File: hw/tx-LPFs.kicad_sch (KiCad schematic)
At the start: 74 parts, among them K1606 G5Q-14-05, K7701 G5Q-14-05, K7702 G5Q-14-05, K7703 G5Q-14-05, K7704 G5Q-14-05, K7705 G5Q-14-05, K7706 G5Q-14-05, K7707 G5Q-14-05, K7708 G5Q-14-05, K7709 G5Q-14-05, U1601 TPIC6C595PWR, U7701 TPIC6C595PWR

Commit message: I think I have finished the relay conversion and 5V SPI I/O expander crap
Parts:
- renumbered C7707 to C7848, C7703 to C7849, C7704 to C7850, C7705 to C7851, C7706 to C7852, C1605 to C7853, C1606 to C7854, C1607 to C7855, C1609 to C7856, C1608 to C7857, C1610 to C7858, C1611 to C7859, C1612 to C7860, C1613 to C7861, C1614 to C7862, C1615 to C7863, C1616 to C7864, C1617 to C7865, C1618 to C7866, C1619 to C7867, C1620 to C7868, C1621 to C7869, C1622 to C7870, C1623 to C7871, C1624 to C7872, C1627 to C7873, C1625 to C7874, C1626 to C7875, C1629 to C7876, C1628 to C7877, C1630 to C7878, C1631 to C7879, C1632 to C7880, C1634 to C7881, C1633 to C7882, C7708 to C7883, C7709 to C7884, C7710 to C7885, C7711 to C7886, C7712 to C7887, C1604 to C7888, C7702 to C7889, K7703 to K7708, K1606 to K7709, K7701 to K7710, K7702 to K7711, K7704 to K7712, K7705 to K7713, K7706 to K7714, K7707 to K7715, K7708 to K7716, K7709 to K7717, L1602 to L7705, L1601 to L7706, L1603 to L7707, L1605 to L7708, L1604 to L7709, L1607 to L7710, L1606 to L7711, L1609 to L7712, L1608 to L7713, L1611 to L7714, L1610 to L7715, L1612 to L7716, L1613 to L7717, L1614 to L7718, L1615 to L7719, L1617 to L7720, L1616 to L7721, L1618 to L7722, L1619 to L7723, L1620 to L7724, U1601 to U7739, U7701 to U7740

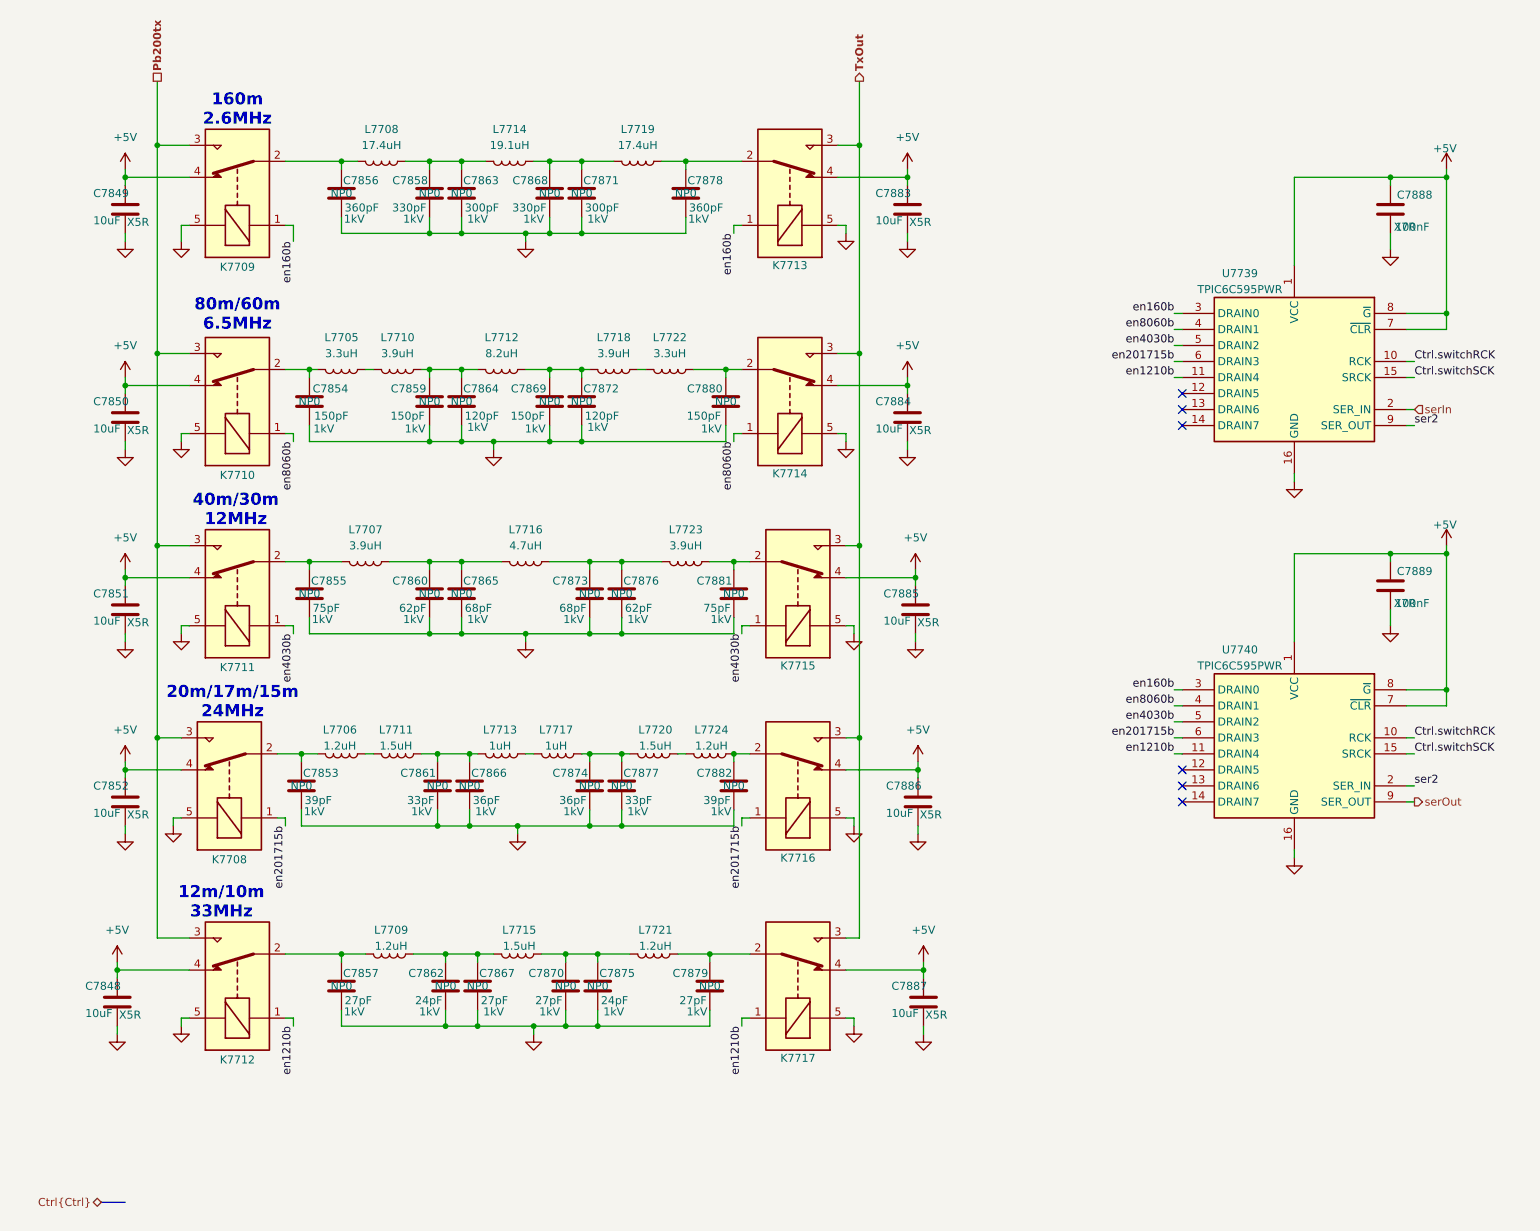
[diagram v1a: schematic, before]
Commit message: Starting to build guanella transformers. Mostly converted to 1-2-1 tx, but FPGA still to do.
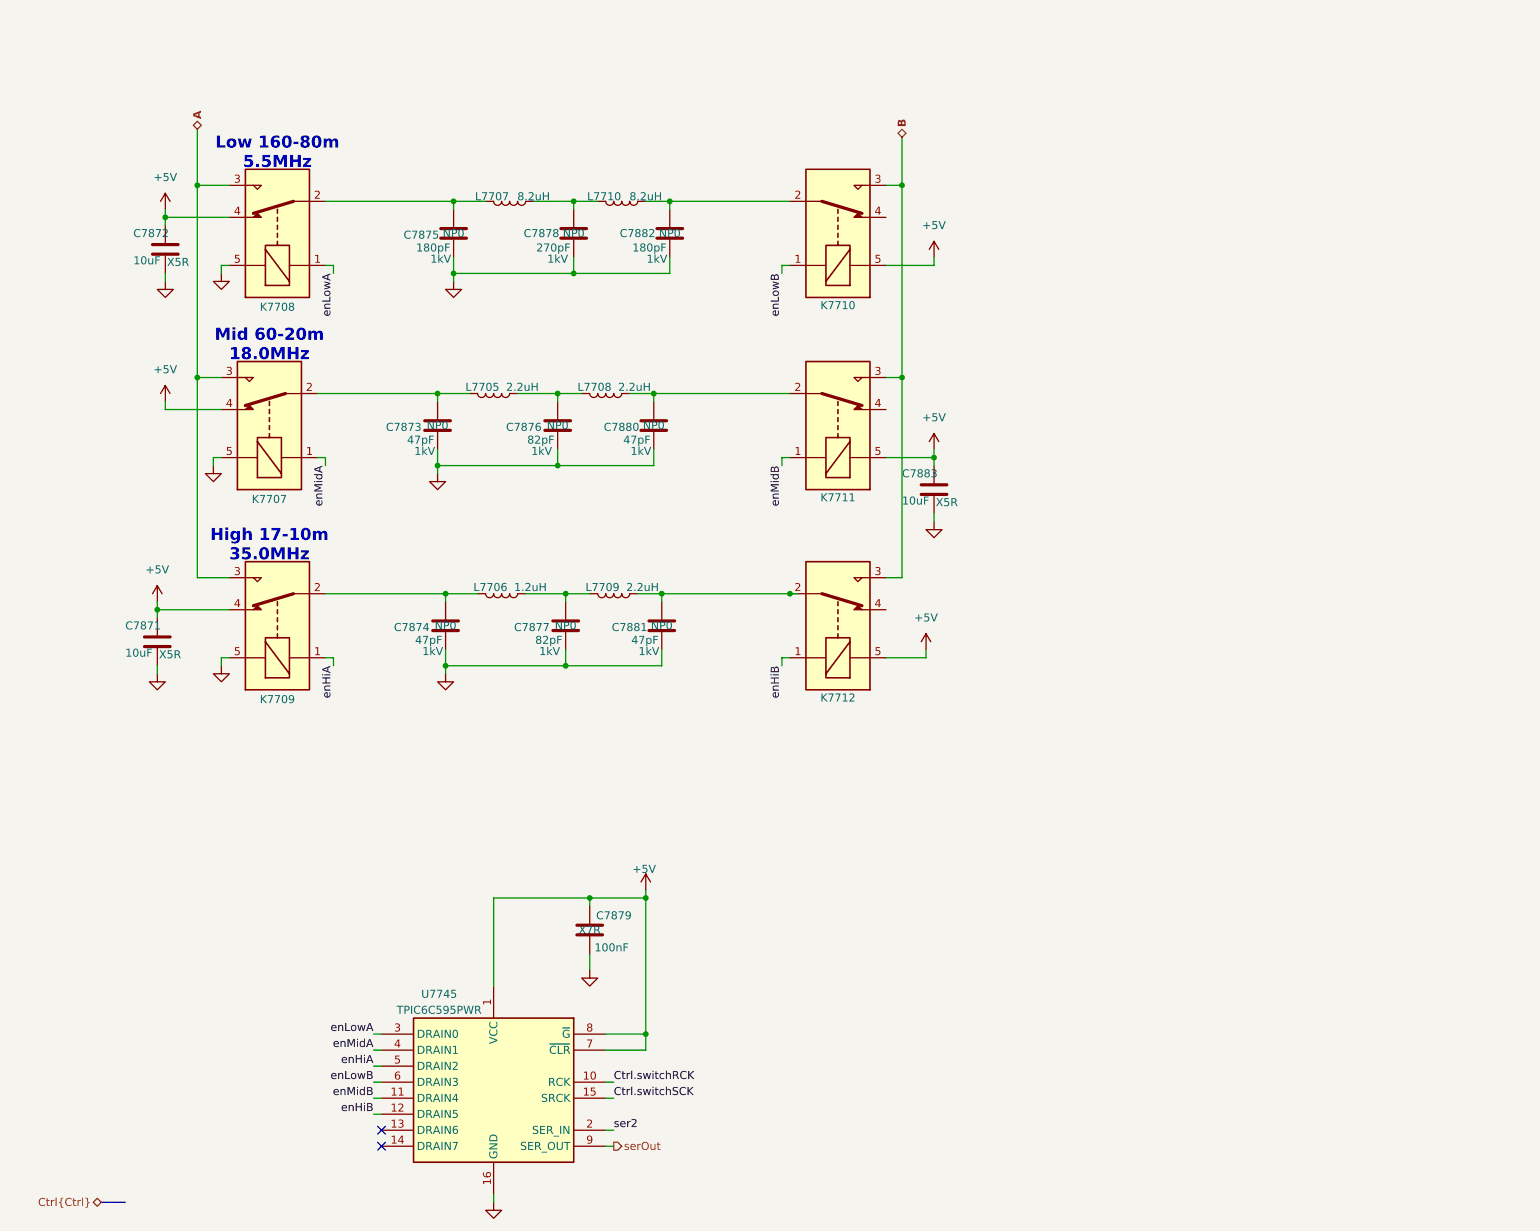
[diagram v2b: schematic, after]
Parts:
- removed C7849, C7850, C7852, C7883, C7884, C7885, C7887: 10uF, Capacitor_SMD:C_0805_2012Metric, symbol Device:C
- removed C7853, C7882: 39pF, Capacitor_SMD:C_0201_0603Metric, symbol Device:C
- removed C7854, C7859, C7869: 150pF, Capacitor_SMD:C_0201_0603Metric, symbol Device:C
- removed C7856, C7878: 360pF, Capacitor_SMD:C_0201_0603Metric, symbol Device:C
- removed C7857, C7867, C7870, C7879: 27pF, Capacitor_SMD:C_0201_0603Metric, symbol Device:C
- removed C7858, C7868: 330pF, Capacitor_SMD:C_0201_0603Metric, symbol Device:C
- removed C7861: 33pF, Capacitor_SMD:C_0201_0603Metric, symbol Device:C
- removed C7862, C7875: 24pF, Capacitor_SMD:C_0201_0603Metric, symbol Device:C
- removed C7863, C7871: 300pF, Capacitor_SMD:C_0201_0603Metric, symbol Device:C
- removed C7864, C7872: 120pF, Capacitor_SMD:C_0201_0603Metric, symbol Device:C
- removed C7865: 68pF, Capacitor_SMD:C_0201_0603Metric, symbol Device:C
- removed C7866: 36pF, Capacitor_SMD:C_0201_0603Metric, symbol Device:C
- removed C7888: 100nF, Capacitor_SMD:C_0805_2012Metric, symbol Device:C
- removed K7709, K7710, K7713, K7714: G5Q-14-05, Relay_THT:Relay_SPDT_Omron-G5Q-1, symbol Relay:G5Q-1
- removed L7710, L7718: 3.9uH, Library:L_Wurth_12.1mm_sq_SMT, symbol Device:L
- removed L7711, L7715, L7720: 1.5uH, Inductor_SMD:L_1812_4532Metric, symbol Device:L
- removed L7712: 8.2uH, Library:L_Wurth_10.9mm_sq_SMT, symbol Device:L
- removed L7713, L7717: 1uH, Inductor_SMD:L_1812_4532Metric, symbol Device:L
- removed L7714: 19.1uH, Library:toroid-inductor-t80-2, symbol Device:L
- removed L7716: 4.7uH, Library:L_Wurth_8.4mm_sq_SMT, symbol Device:L
- removed L7719: 17.4uH, Library:toroid-inductor-t80-2, symbol Device:L
- removed L7721, L7724: 1.2uH, Inductor_SMD:L_1812_4532Metric, symbol Device:L
- removed L7722: 3.3uH, Library:L_Wurth_8.4mm_sq_SMT, symbol Device:L
- removed U7739: TPIC6C595PWR, SOP65P640X120-16N, symbol Library:TPIC6C595PWR
- added C7881: 47pF, Capacitor_SMD:C_0201_0603Metric, symbol Device:C
- C7873: value 68pF -> 47pF
- C7874: value 36pF -> 47pF
- C7875: renamed from C7855; value 75pF -> 180pF
- C7876: value 62pF -> 82pF
- C7877: value 33pF -> 82pF
- C7878: renamed from C7860; value 62pF -> 270pF
- C7880: value 150pF -> 47pF
- C7882: renamed from C7881; value 75pF -> 180pF
- L7705: value 3.3uH -> 2.2uH; footprint Library:L_Wurth_8.4mm_sq_SMT -> Library:L_Wurth_12.1mm_sq_SMT; MP 7443340330 -> 7443310390
- L7706: footprint Inductor_SMD:L_1812_4532Metric -> Library:L_Wurth_12.1mm_sq_SMT; MF Coilcraft -> Wurth; MP 1812FS-122JR_ -> 7443310390
- L7707: value 3.9uH -> 8.2uH
- L7708: value 17.4uH -> 2.2uH; footprint Library:toroid-inductor-t80-2 -> Library:L_Wurth_12.1mm_sq_SMT; MF (none) -> Wurth; MP (none) -> 7443310390
- L7709: value 1.2uH -> 2.2uH; footprint Inductor_SMD:L_1812_4532Metric -> Library:L_Wurth_12.1mm_sq_SMT; MF Coilcraft -> Wurth; MP 1812FS-122JR -> 7443310390; Mfg Wurth -> (none); MfgPart 74433300180 -> (none)
- L7710: renamed from L7723; value 3.9uH -> 8.2uH
- renumbered C7848 to C7871, C7851 to C7872, C7889 to C7879, C7886 to C7883, K7708 to K7707, K7711 to K7708, K7712 to K7709, K7715 to K7710, K7716 to K7711, K7717 to K7712, U7740 to U7745
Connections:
- net +5V: now also K7710.5, K7711.5, K7712.5; no longer K7710.4, K7711.4, K7712.4
- net GND: now also C7881.2; no longer K7710.5, K7711.5, K7712.5
- net at K7712.2: now also L7709.2, C7881.1
- net at C7878.1, L7707.2: now also L7710.1
- net at C7877.1: now also L7706.2, L7709.1; no longer C7874.1
- net enHiB: now reaches U7745.12 (DRAIN5)
- net enHiB: now also K7712.1
- net at K7709.2: now also C7874.1, L7706.1; no longer L7709.1
- net at K7711.2: now also C7880.1, L7708.2
- net at L7708.1: now also C7876.1, L7705.2
- net at L7705.1: now also C7873.1, K7707.2
- net Pb200tx renamed A
- net TxOut renamed B
- removed net en1210b: K7709.1, K7712.1, U7745.11 (DRAIN4)
- net en160b renamed enLowA
- net enLowA: now also K7708.1
- removed net en201715b: K7707.1, K7711.1, U7745.6 (DRAIN3)
- removed net en4030b: K7708.1, K7710.1, U7745.5 (DRAIN2)
- net en8060b renamed enMidA
- net enMidA: now also K7707.1
- new net enHiA: K7709.1, U7745.5 (DRAIN2)
- new net enLowB: K7710.1, U7745.6 (DRAIN3)
- new net enMidB: K7711.1, U7745.11 (DRAIN4)
- no-connect marks 6 -> 2
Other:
- note added: "High 17-10m 35.0MHz"
- note added: "Low 160-80m 5.5MHz"
- note added: "Mid 60-20m 18.0MHz"
- note removed: "12m/10m 33MHz"
- note removed: "160m 2.6MHz"
- note removed: "20m/17m/15m 24MHz"
- note removed: "40m/30m 12MHz"
- note removed: "80m/60m 6.5MHz"
- moved on the sheet: C7871, C7872, C7875, C7878, C7879, C7882, C7883, K7707, K7708, K7709, K7710, K7711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

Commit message: Checkpoint. FPGA is mostly done (need a check!). Working on new LPFs. Need inductor footprints and to fix a bunch of broken/missing footprints.
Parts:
- C7873, C7875, C7876, C7878, C7880, C7882: footprint Capacitor_SMD:C_0201_0603Metric -> Capacitor_SMD:C_0603_1608Metric
- C7874, C7881: value 47pF -> 27pF; footprint Capacitor_SMD:C_0201_0603Metric -> Capacitor_SMD:C_0603_1608Metric
- C7877: value 82pF -> 47pF; footprint Capacitor_SMD:C_0201_0603Metric -> Capacitor_SMD:C_0603_1608Metric
- C7879: footprint Capacitor_SMD:C_0805_2012Metric -> Capacitor_SMD:C_0603_1608Metric
- L7705, L7706, L7708: footprint Library:L_Wurth_12.1mm_sq_SMT -> (none)
- L7707, L7710: footprint Library:L_Wurth_12.1mm_sq_SMT -> (none); MF Wurth -> (none); MP 7443310390 -> (none)
- L7709: value 2.2uH -> 1.2uH; footprint Library:L_Wurth_12.1mm_sq_SMT -> (none)

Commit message: OK I have part numbers for consolidated caps, resistors, inductors and all ICs are now Uxxx refdes.
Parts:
- C7882: renamed from C7871; footprint Capacitor_SMD:C_0805_2012Metric -> Capacitor_SMD:C_0603_1608Metric; Manufacturer_Name (none) -> Taoup Uidem; Manufacturer_Part_Number (none) -> 81-GXT155R71E223KE1D; Mouser Part Number (none) -> 963-MLAST168BB5106MT; working-voltage 10V -> 25V
- C7883: renamed from C7872; footprint Capacitor_SMD:C_0805_2012Metric -> Capacitor_SMD:C_0603_1608Metric; Manufacturer_Name (none) -> Taoup Uidem; Manufacturer_Part_Number (none) -> 81-GXT155R71E223KE1D; Mouser Part Number (none) -> 963-MLAST168BB5106MT; working-voltage 10V -> 25V
- C7884: renamed from C7873; footprint Capacitor_SMD:C_0603_1608Metric -> Capacitor_SMD:C_0805_2012Metric; Manufacturer_Name (none) -> YAGEO; Manufacturer_Part_Number (none) -> CC0805JRNPOCBN470; Mouser Part Number (none) -> 603-CC0805JRCBN470
- C7885: renamed from C7874; footprint Capacitor_SMD:C_0603_1608Metric -> Capacitor_SMD:C_0805_2012Metric; Manufacturer_Name (none) -> Kyocera AVX; Manufacturer_Part_Number (none) -> KGM21ECG3A270JU; Mouser Part Number (none) -> 581-KGM21ECG3A270JU
- C7886: renamed from C7875; footprint Capacitor_SMD:C_0603_1608Metric -> Capacitor_SMD:C_0805_2012Metric; Manufacturer_Name (none) -> KEMET; Manufacturer_Part_Number (none) -> C0805C181JDGACAUTO; Mouser Part Number (none) -> 80-C0805C181JDGACATO
- C7887: renamed from C7876; footprint Capacitor_SMD:C_0603_1608Metric -> Capacitor_SMD:C_0805_2012Metric; Manufacturer_Name (none) -> KEMET; Manufacturer_Part_Number (none) -> C0805C820JDGACTU; Mouser Part Number (none) -> 80-C0805C820JDG
- C7888: renamed from C7877; footprint Capacitor_SMD:C_0603_1608Metric -> Capacitor_SMD:C_0805_2012Metric; Manufacturer_Name (none) -> YAGEO; Manufacturer_Part_Number (none) -> CC0805JRNPOCBN470; Mouser Part Number (none) -> 603-CC0805JRCBN470
- C7889: renamed from C7878; Manufacturer_Name (none) -> TDK; Manufacturer_Part_Number (none) -> CGA3E2C0G1H271J080AA; Mouser Part Number (none) -> 810-CGA3E2C0G1H271J
- C7890: renamed from C7879; Manufacturer_Name (none) -> Kemet; Manufacturer_Part_Number (none) -> C0805F104K1RACAUTO; Mouser Part Number (none) -> 80-C0805F104K1RAUTO
- C7891: renamed from C7880; footprint Capacitor_SMD:C_0603_1608Metric -> Capacitor_SMD:C_0805_2012Metric; Manufacturer_Name (none) -> YAGEO; Manufacturer_Part_Number (none) -> CC0805JRNPOCBN470; Mouser Part Number (none) -> 603-CC0805JRCBN470
- C7892: renamed from C7881; footprint Capacitor_SMD:C_0603_1608Metric -> Capacitor_SMD:C_0805_2012Metric; Manufacturer_Name (none) -> Kyocera AVX; Manufacturer_Part_Number (none) -> KGM21ECG3A270JU; Mouser Part Number (none) -> 581-KGM21ECG3A270JU
- C7893: renamed from C7882; footprint Capacitor_SMD:C_0603_1608Metric -> Capacitor_SMD:C_0805_2012Metric; Manufacturer_Name (none) -> KEMET; Manufacturer_Part_Number (none) -> C0805C181JDGACAUTO; Mouser Part Number (none) -> 80-C0805C181JDGACATO
- C7894: renamed from C7883; footprint Capacitor_SMD:C_0805_2012Metric -> Capacitor_SMD:C_0603_1608Metric; Manufacturer_Name (none) -> Taoup Uidem; Manufacturer_Part_Number (none) -> 81-GXT155R71E223KE1D; Mouser Part Number (none) -> 963-MLAST168BB5106MT; working-voltage 10V -> 25V
- renumbered U7745 to U7744

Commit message: checkpoint to merge
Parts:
- L7705, L7707, L7708, L7710: footprint (none) -> Library:T68-toroid-1
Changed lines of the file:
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@@
 			)
 		)
-		(property "Footprint" ""
+		(property "Footprint" "Library:T68-toroid-1"
 			(at 86.36 71.12 0)
 			(effects
@@
 			)
 		)
-		(property "Description" "2.2uH T68-6 22t #18AWG"
+		(property "Description" "2.2uH T68-6 22t #22AWG"
 			(at 86.36 71.12 0)
 			(effects
@@
 			)
 		)
-		(property "Footprint" ""
+		(property "Footprint" "Library:T68-toroid-1"
 			(at 106.68 40.64 0)
 			(effects
@@
 			)
 		)
-		(property "Description" "T68-2 38t #18AWG"
+		(property "Description" "T68-2 38t #22AWG"
 			(at 106.68 40.64 0)
 			(effects
@@
 			)
 		)
-		(property "Footprint" ""
+		(property "Footprint" "Library:T68-toroid-1"
 			(at 88.9 40.64 0)
 			(effects
@@
 			)
 		)
-		(property "Description" "T68-2 38t #18AWG"
+		(property "Description" "T68-2 38t #22AWG"
 			(at 88.9 40.64 0)
 			(effects
@@
 			)
 		)
-		(property "Footprint" ""
+		(property "Footprint" "Library:T68-toroid-1"
 			(at 104.14 71.12 0)
 			(effects
@@
 			)
 		)
-		(property "Description" "2.2uH T68-6 22t #18AWG"
+		(property "Description" "2.2uH T68-6 22t #22AWG"
 			(at 104.14 71.12 0)
 			(effects

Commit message: Clean up some footprints no longer used. Build footprints for LPF and antenna tuner inductors.
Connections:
- net ser2 renamed serIn
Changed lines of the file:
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@@
 	)
 	(junction
-		(at 133.35 102.87)
-		(diameter 0)
-		(color 0 0 0 0)
-	)
-	(junction
 		(at 111.76 71.12)
 		(diameter 0)
@@
 	(wire
 		(pts
-			(xy 133.35 102.87) (xy 134.62 102.87)
-		)
-		(stroke
-			(width 0)
-			(type default)
-		)
-	)
-	(wire
-		(pts
 			(xy 39.37 38.1) (xy 44.45 38.1)
 		)
@@
 		)
 	)
-	(label "ser2"
-		(at 105.41 187.96 0)
-		(effects
-			(font
-				(size 1.27 1.27)
-			)
-			(justify left bottom)
-		)
-	)
 	(label "enMidA"
 		(at 59.69 82.55 270)
@@
 		)
 	)
+	(hierarchical_label "serIn"
+		(shape input)
+		(at 105.41 187.96 0)
+		(effects
+			(font
+				(size 1.27 1.27)
+			)
+			(justify left)
+		)
+	)
 	(hierarchical_label "Ctrl{Ctrl}"
 		(shape bidirectional)
@@
 			)
 		)
-		(property "Description" "12t #14AWG on 0.5in close wound."
+		(property "Description" "16t #22AWG on T68-6 core."
 			(at 105.41 102.87 0)
 			(effects
@@
 			)
 		)
-		(property "Description" "12t #14AWG on 0.5in close wound."
+		(property "Description" "16t #22AWG on T68-6 core."
 			(at 87.63 102.87 0)
 			(effects

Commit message: All symbols and footprints seem right now, and schematic again imports into PCB without error
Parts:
- L7705, L7707, L7708, L7710: footprint Library:T68-toroid-1 -> Library:T68-toroid-1-rolling-tire
- L7706, L7709: footprint (none) -> Library:T68-toroid-1-rolling-tire
- renumbered C7882 to C7881, C7883 to C7882, C7884 to C7883, C7885 to C7884, C7886 to C7885, C7887 to C7886, C7888 to C7887, C7889 to C7888, C7890 to C7889, C7891 to C7890, C7892 to C7891, C7893 to C7892, C7894 to C7893, U7744 to U7743

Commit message: I'm thinking I might make a NexRx with just the rx portion of this design first to test my skills and capabilities.
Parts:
- renumbered C7881 to C7880, C7882 to C7881, C7883 to C7882, C7884 to C7883, C7885 to C7884, C7886 to C7885, C7887 to C7886, C7888 to C7887, C7889 to C7888, C7890 to C7889, C7891 to C7890, C7892 to C7891, C7893 to C7892, K7707 to K7704, K7708 to K7705, K7709 to K7706, K7710 to K7707, K7711 to K7708, K7712 to K7709
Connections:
- net +5V: now also K7704.5, K7705.5, K7706.5; no longer K7704.4, K7705.4, K7706.4
- net GND: now also K7704.4, K7705.4, K7706.4, K7707.4, K7708.4, K7709.4; no longer K7704.5, K7705.5, K7706.5
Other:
- moved on the sheet: C7880, C7881, C7892
